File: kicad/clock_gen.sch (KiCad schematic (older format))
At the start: 20 parts, among them J1 Programming, SW1 Rotary_Encoder, SW2 Rotary_Encoder, U1 MachXO2-1200-QFN32, U2 LM3480-3.3, U3 74HCT541, X1 DSC1001AE5-001.2000

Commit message: Finished PCB
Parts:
- removed SW1, SW2: Rotary_Encoder, Potentiometer_THT:Potentiometer_Bourns_PTV09A-2_Single_Horizontal, symbol Device:Rotary_Encoder
- removed U2: LM3480-3.3, Package_TO_SOT_SMD:SOT-23, symbol Regulator_Linear:LM3480-3.3
- added C12: 1uF, Capacitor_SMD:C_0603_1608Metric, symbol Device:C
- added D1: IN-S63AT5G, LED_SMD:LED_0603_1608Metric, symbol Device:LED
- added D2: LTST-C190KRKT, LED_SMD:LED_0603_1608Metric, symbol Device:LED
- added J2: buf_output, Connector_PinHeader_1.27mm:PinHeader_1x08_P1.27mm_Vertical, symbol Connector:Conn_01x08_Male
- added J3: Power, Connector_PinHeader_1.27mm:PinHeader_1x03_P1.27mm_Vertical, symbol Connector:Conn_01x03_Male
- added J4: CLRN, Connector_PinHeader_1.27mm:PinHeader_1x01_P1.27mm_Vertical, symbol Connector:Conn_01x01_Female
- added LOGO1: Logo_Open_Hardware_Large, logo:clk, symbol Graphic:Logo_Open_Hardware_Large
- added R2, R3: 1k, Resistor_SMD:R_0603_1608Metric, symbol Device:R
- added SW1, SW2: Rotary_Encoder, Connector_PinHeader_1.27mm:PinHeader_1x03_P1.27mm_Vertical, symbol Connector:Conn_01x03_Male
- added U2: MIC5504-3.3YM5, Package_TO_SOT_SMD:SOT-23-5, symbol Regulator_Linear:MIC5504-3.3YM5
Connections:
- net PB11A is gone; now on net clk_1M2: U1.13 (PB11A)
- net PB4C/CS is gone; now on net clk_20k: U1.8 (PB4C/CS)
- net PB6C/SCLK is gone; now on net clk_40k: U1.9 (PB6C/SCLK)
- net PB6D/MISO is gone; now on net clk_60k: U1.10 (PB6D/MISO)
- net PB9A is gone; now on net clk_80k: U1.11 (PB9A)
- net PB9B is gone; now on net clk_100k: U1.12 (PB9B)
- net PL9A is gone; now on net pin2: U1.4 (PL9A)
- net PL9B is gone; now on net Blanking: U1.5 (PL9B)
- net PT12C/SCL is gone; now on net pin1: U1.28 (PT12C/SCL)
- net +3V3: now also X1.1 (EN), X1.4 (Vdd), C12.1, J3.3 (Pin_3), R2.1, R3.1, U2.5 (VOUT); no longer L1.1
- net GND: now also U3.1 (G1), U3.10 (GND), U3.19 (G2), X1.2 (GND), C12.2, D1.1 (K), J3.2 (Pin_2), SW1.2 (Pin_2), SW2.2 (Pin_2), U2.2 (GND)
- net clk_1M2: now reaches X1.3 (OUT)
- net at U3.11 (Y7): now also J2.8 (Pin_8)
- net at U3.12 (Y6): now also J2.7 (Pin_7)
- net at U3.13 (Y5): now also J2.6 (Pin_6)
- net at U3.14 (Y4): now also J2.5 (Pin_5)
- net at U3.15 (Y3): now also J2.4 (Pin_4)
- net at U3.16 (Y2): now also J2.3 (Pin_3)
- net at U3.17 (Y1): now also J2.2 (Pin_2)
- net at U3.18 (Y0): now also J2.1 (Pin_1)
- net clk_100k: now reaches U3.2 (A0)
- net +5V: now reaches U3.20 (VCC)
- net +5V: now also L1.1, U2.1 (VIN), U2.3 (EN)
- net clk_80k: now reaches U3.3 (A1)
- net clk_60k: now reaches U3.4 (A2)
- net clk_40k: now reaches U3.5 (A3)
- net clk_20k: now reaches U3.6 (A4)
- net Blanking: now reaches U3.7 (A5)
- net pin2: now reaches U3.8 (A6)
- net pin1: now reaches U3.9 (A7)
- net EXT3v3 renamed EXT5v
- net EXT5v: now also J3.1 (Pin_1)
- net PB11B renamed clrn
- net clrn: now also J4.1 (Pin_1)
- net PB20C/SN renamed E1A
- net E1A: now also SW1.1 (Pin_1)
- net PB20D/MOSI renamed E1B
- net E1B: now also SW1.3 (Pin_3)
- net PR5C renamed E2B
- net E2B: now also SW2.3 (Pin_3)
- net PR5D renamed E2A
- net E2A: now also SW2.1 (Pin_1)
- net PT12D/SDA: no longer names the net of U1.27 (PT12D/SDA)
- net PT15C/JTAGENB: no longer names the net of U1.26 (PT15C/JTAGENB)
- net PT15D/PROGRAMN: no longer names the net of U1.25 (PT15D/PROGRAMN)
- net PT17D/DONE renamed led
- net led: now also D2.1 (K)
- new net: D1.2 (A), R2.2
- new net: D2.2 (A), R3.2
- no-connect marks 0 -> 3
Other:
- moved on the sheet: C1, C10, C11, C2, C3, C4, C5, C6, C7, C8, C9, L1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

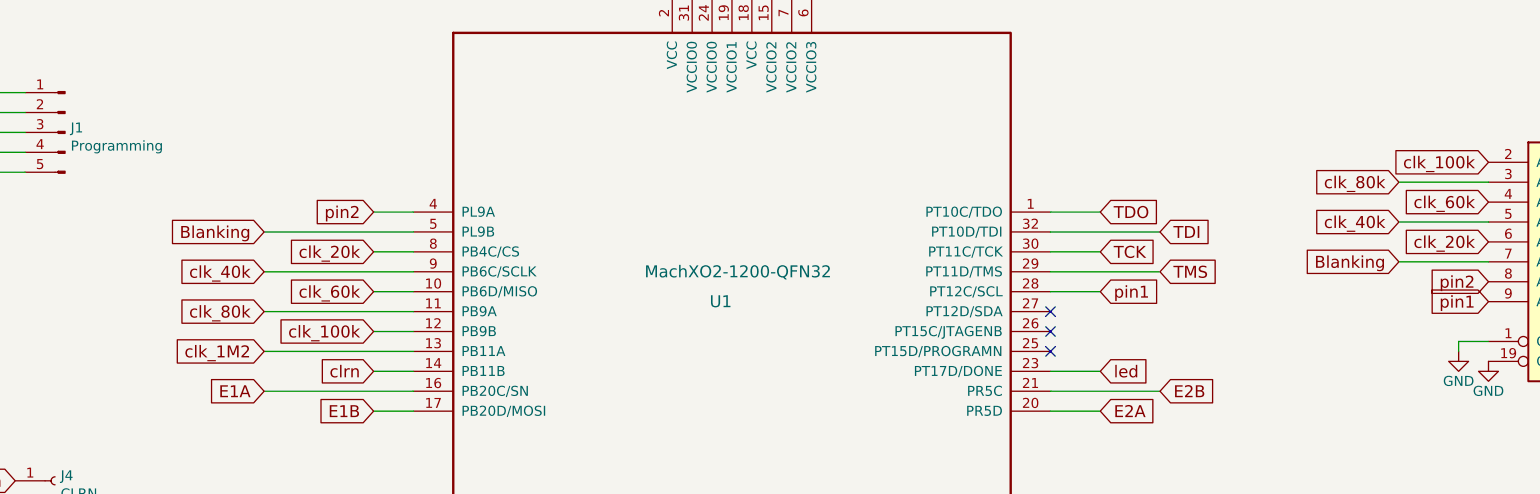
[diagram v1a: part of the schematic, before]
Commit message: clock gen Minimal Working Example (tested)
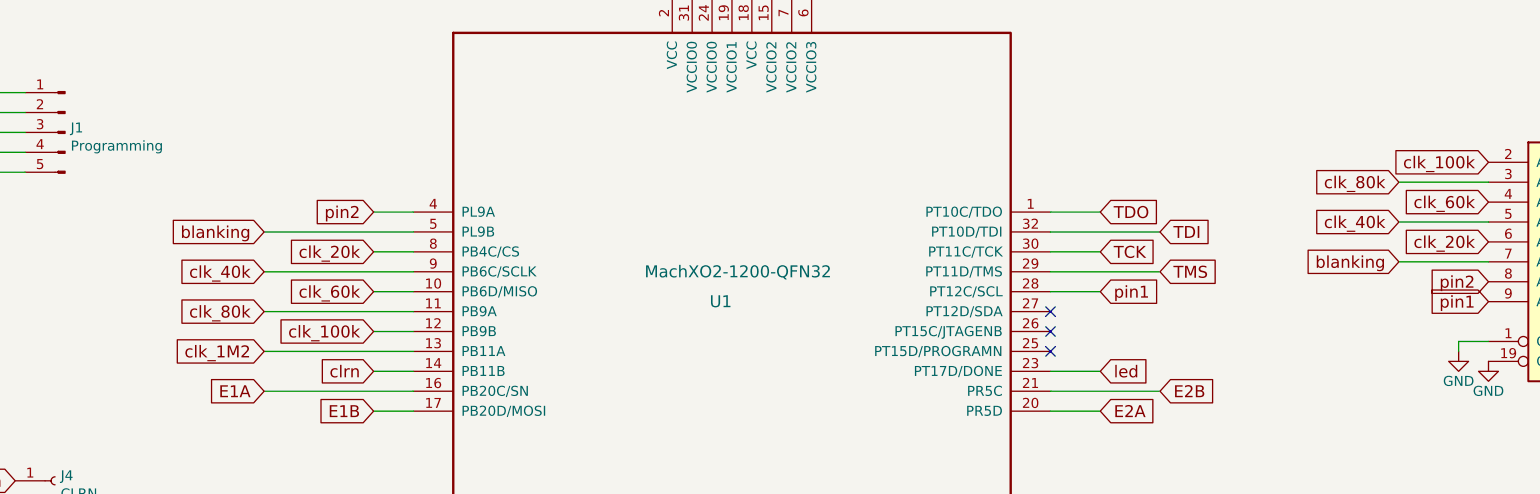
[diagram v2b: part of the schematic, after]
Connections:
- net Blanking renamed blanking
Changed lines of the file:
@@
 EESchema Schematic File Version 4
-LIBS:clock_gen-cache
-EELAYER 26 0
+EELAYER 30 0
 EELAYER END
 $Descr A4 11693 8268
@@
 pin2
 Text GLabel 8800 4550 0    60   Input ~ 0
-Blanking
+blanking
 Text GLabel 9250 4450 0    60   Input ~ 0
 clk_20k
@@
 pin2
 Text GLabel 3100 4400 0    60   Input ~ 0
-Blanking
+blanking
 Text GLabel 3650 4500 0    60   Input ~ 0
 clk_20k
